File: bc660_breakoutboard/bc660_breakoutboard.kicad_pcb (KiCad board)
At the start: 2 copper layers, 22 parts, among them J2 Conn_01x12_Pin, J4 SIM8051-6-0-14-01-X-REVD, U1 BC660K-GL, U2 ESDS304DBVR

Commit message: update pcb design
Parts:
- added J1: SMA_CONNECTOR, SMA_CONNECTOR:LPRS_SMA_CONNECTOR, F.Cu at (125.4, 68.7)
- added J3: Conn_01x02_Pin, Connector_PinHeader_2.54mm:PinHeader_1x02_P2.54mm_Vertical, F.Cu at (101.3, 63.2)
- added J5: Conn_01x02_Pin, Connector_PinHeader_2.54mm:PinHeader_1x02_P2.54mm_Vertical, F.Cu at (112.8, 63.2)
- added J6: Conn_01x06_Pin, Connector_PinHeader_2.54mm:PinHeader_1x06_P2.54mm_Vertical, F.Cu at (103.9, 103.9)
- J2: value Conn_01x12_Pin -> Conn_01x01_Pin; footprint Connector_PinHeader_2.54mm:PinHeader_1x12_P2.54mm_Vertical -> Connector_PinHeader_2.54mm:PinHeader_1x01_P2.54mm_Vertical
- moved C6 85.1 mm to (107.1, 67.0), turned to -90 degrees
- moved C7 83.8 mm to (104.1, 67.0), turned to -90 degrees
- moved C8 82.7 mm to (101.1, 67.0), turned to -90 degrees
- moved C9 81.8 mm to (98.0, 67.0), turned to -90 degrees
- moved J2 68.7 mm to (92.2, 72.1), turned to 90 degrees
- moved C4 64.7 mm to (95.2, 94.0), turned to -90 degrees
- moved C5 57.8 mm to (88.4, 97.3), turned to -90 degrees
- moved J4 51.9 mm to (81.0, 88.4)
- moved C3 51.2 mm to (81.0, 105.2), turned to -90 degrees
- moved R4 33.2 mm to (72.4, 83.3)
- moved R2 32.3 mm to (81.0, 101.1), turned to 90 degrees
- moved R8 31.0 mm to (110.1, 67.1), turned to -90 degrees
- moved C2 30.8 mm to (75.7, 79.5), turned to 90 degrees
- moved R7 28.8 mm to (113.0, 67.1), turned to -90 degrees
- moved R1 27.1 mm to (78.5, 79.5), turned to -90 degrees
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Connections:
- C6 pad 2: Net-(J2-Pin_1) -> Net-(J3-Pin_2)
- C7 pad 2: Net-(J2-Pin_1) -> Net-(J3-Pin_2)
- C8 pad 2: Net-(J2-Pin_1) -> Net-(J3-Pin_2)
- C9 pad 2: Net-(J2-Pin_1) -> Net-(J3-Pin_2)
- R5 pad 1: Net-(J2-Pin_2) -> Net-(J6-Pin_4)
- R6 pad 1: Net-(J2-Pin_3) -> Net-(J6-Pin_3)
- R7 pad 1: Net-(J2-Pin_4) -> Net-(J5-Pin_1)
- R8 pad 1: Net-(J2-Pin_5) -> Net-(J5-Pin_2)
- R9 pad 2: Net-(J2-Pin_6) -> Net-(J6-Pin_6)
- U1 pad 15: Net-(J2-Pin_8) -> Net-(J6-Pin_1)
- U1 pad 16: GND -> Net-(J6-Pin_2)
- U1 pad 19: Net-(J2-Pin_9) -> Net-(J6-Pin_5)
- U1 pad 24: Net-(J2-Pin_10) -> unconnected-(U1-VDD_EXT-Pad24)
- U1 pad 42: Net-(J2-Pin_1) -> Net-(J3-Pin_2)
- U1 pad 43: Net-(J2-Pin_1) -> Net-(J3-Pin_2)
- U1 pad 7: Net-(J2-Pin_7) -> Net-(J2-Pin_1)
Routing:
- net Net-(U1-USIM_RST): track 0.00 -> 89.9 mm
- net Net-(J4-GND): track 0.00 -> 61.2 mm
- net Net-(J4-VCC): track 0.00 -> 50.2 mm
- net Net-(U1-USIM_DATA): track 0.00 -> 38.5 mm
- net Net-(J4-CLK): track 0.00 -> 22.7 mm
- net Net-(J3-Pin_2): track 0.00 -> 21.7 mm
- net Net-(J4-I/O): track 0.00 -> 19.3 mm
- net Net-(U1-USIM_CLK): track 0.00 -> 19.2 mm
- net Net-(J6-Pin_5): track 0.00 -> 15.0 mm
- net Net-(J2-Pin_1): track 0.00 -> 14.3 mm
- net Net-(J6-Pin_1): track 0.00 -> 14.2 mm
- net Net-(J6-Pin_2): track 0.00 -> 13.6 mm
- net Net-(U1-ANT_RF): track 0.00 -> 11.8 mm
- net Net-(U1-RI): track 0.00 -> 10.2 mm
- net Net-(U1-MAIN_RXD): track 0.00 -> 9.05 mm
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- added copper zone on B.Cu, net GND
- added copper zone on F.Cu, net GND
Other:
- board outline added: 59.7 x 48.5 mm

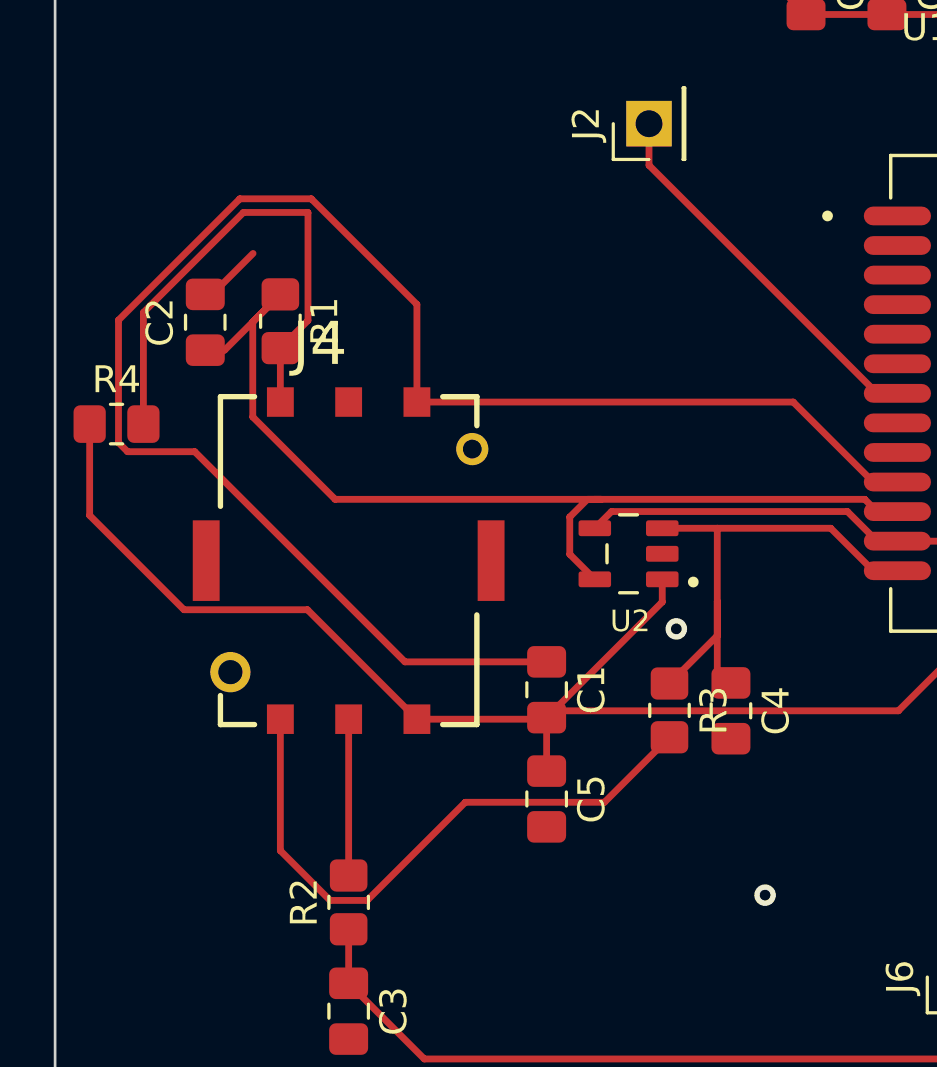
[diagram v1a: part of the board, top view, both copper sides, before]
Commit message: update pcb breakoutboard
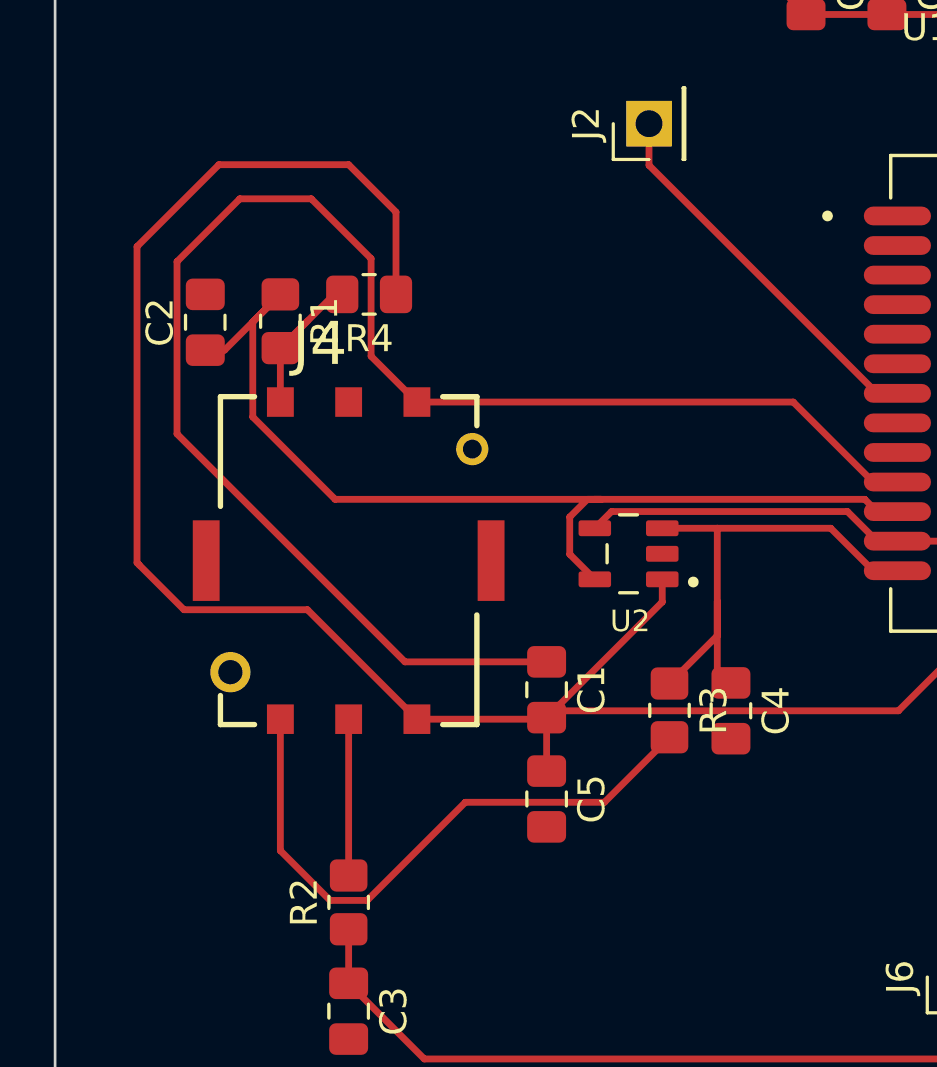
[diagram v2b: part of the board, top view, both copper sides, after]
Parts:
- moved R4 10.6 mm to (81.8, 78.5), turned to 180 degrees
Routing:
- net Net-(J4-VCC): track 50.2 -> 70.8 mm
- net Net-(J4-I/O): track 19.3 -> 6.59 mm
- net Net-(J4-GND): track 61.2 -> 57.9 mm
- net GND: track 5.42 -> 3.26 mm, vias 2 -> 0
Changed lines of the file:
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@@
   )
   (footprint "Resistor_SMD:R_0805_2012Metric_Pad1.20x1.40mm_HandSolder" (layer "F.Cu")
-    (at 72.39 83.312)
+    (at 81.788 78.486 180)
     (descr "Resistor SMD 0805 (2012 Metric), square (rectangular) end terminal, IPC_7351 nominal with elongated pad for handsoldering. (Body size source: IPC-SM-782 page 72, https://www.pcb-3d.com/wordpress/wp-content/uploads/ipc-sm-782a_amendment_1_and_2.pdf), generated with kicad-footprint-generator")
     (tags "resistor handsolder")
@@
     (fp_line (start 1 0.625) (end -1 0.625)
       (stroke (width 0.1) (type solid)) (layer "F.Fab"))
-    (pad "1" smd roundrect (at -1 0) (size 1.2 1.4) (layers "F.Cu" "F.Paste" "F.Mask") (roundrect_rratio 0.208333)
+    (pad "1" smd roundrect (at -1 0 180) (size 1.2 1.4) (layers "F.Cu" "F.Paste" "F.Mask") (roundrect_rratio 0.208333)
       (net 2 "Net-(J4-VCC)") (pintype "passive"))
-    (pad "2" smd roundrect (at 1 0) (size 1.2 1.4) (layers "F.Cu" "F.Paste" "F.Mask") (roundrect_rratio 0.208333)
+    (pad "2" smd roundrect (at 1 0 180) (size 1.2 1.4) (layers "F.Cu" "F.Paste" "F.Mask") (roundrect_rratio 0.208333)
       (net 45 "Net-(J4-I{slash}O)") (pintype "passive"))
     (model "${KICAD6_3DMODEL_DIR}/Resistor_SMD.3dshapes/R_0805_2012Metric.wrl"
@@
     (stroke (width 0.1) (type default)) (fill none) (layer "Edge.Cuts"))
   (segment (start 101.444 85.468) (end 100.544 85.468) (width 0.254) (layer "F.Cu") (net 1))
-  (segment (start 72.463 84.001001) (end 72.463 79.444447) (width 0.254) (layer "F.Cu") (net 1))
-  (segment (start 83.120999 92.159) (end 75.300999 84.339) (width 0.254) (layer "F.Cu") (net 1))
-  (segment (start 79.636052 74.93) (end 83.566 78.859948) (width 0.254) (layer "F.Cu") (net 1))
-  (segment (start 88.392 92.159) (end 83.120999 92.159) (width 0.254) (layer "F.Cu") (net 1))
-  (segment (start 72.800999 84.339) (end 72.463 84.001001) (width 0.254) (layer "F.Cu") (net 1))
+  (segment (start 79.636052 74.93) (end 76.977447 74.93) (width 0.254) (layer "F.Cu") (net 1))
+  (segment (start 83.120999 92.159) (end 88.392 92.159) (width 0.254) (layer "F.Cu") (net 1))
+  (segment (start 74.64 77.267448) (end 74.64 83.678) (width 0.254) (layer "F.Cu") (net 1))
+  (segment (start 76.977447 74.93) (end 74.64 77.267448) (width 0.254) (layer "F.Cu") (net 1))
+  (segment (start 81.861 77.154948) (end 79.636052 74.93) (width 0.254) (layer "F.Cu") (net 1))
+  (segment (start 81.861 80.787) (end 81.861 77.154948) (width 0.254) (layer "F.Cu") (net 1))
   (segment (start 100.544 85.468) (end 97.568 82.492) (width 0.254) (layer "F.Cu") (net 1))
-  (segment (start 75.300999 84.339) (end 72.800999 84.339) (width 0.254) (layer "F.Cu") (net 1))
-  (segment (start 72.463 79.444447) (end 76.977447 74.93) (width 0.254) (layer "F.Cu") (net 1))
+  (segment (start 74.64 83.678) (end 83.120999 92.159) (width 0.254) (layer "F.Cu") (net 1))
+  (segment (start 83.566 82.492) (end 81.861 80.787) (width 0.254) (layer "F.Cu") (net 1))
   (segment (start 97.568 82.492) (end 83.566 82.492) (width 0.254) (layer "F.Cu") (net 1))
-  (segment (start 83.566 78.859948) (end 83.566 82.492) (width 0.254) (layer "F.Cu") (net 1))
-  (segment (start 76.977447 74.93) (end 79.636052 74.93) (width 0.254) (layer "F.Cu") (net 1))
+  (segment (start 81.026 73.66) (end 82.788 75.422) (width 0.254) (layer "F.Cu") (net 2))
   (segment (start 88.392 94.234) (end 88.392 96.223) (width 0.254) (layer "F.Cu") (net 2))
   (segment (start 88.334 94.292) (end 88.392 94.234) (width 0.254) (layer "F.Cu") (net 2))
   (segment (start 88.646 93.98) (end 88.392 94.234) (width 0.254) (layer "F.Cu") (net 2))
   (segment (start 92.695 89.931) (end 88.392 94.234) (width 0.254) (layer "F.Cu") (net 2))
+  (segment (start 73.239 88.559) (end 73.152 88.472) (width 0.254) (layer "F.Cu") (net 2))
   (segment (start 83.566 94.292) (end 79.493 90.219) (width 0.254) (layer "F.Cu") (net 2))
+  (segment (start 74.899 90.219) (end 73.239 88.559) (width 0.254) (layer "F.Cu") (net 2))
   (segment (start 101.482 93.98) (end 88.646 93.98) (width 0.254) (layer "F.Cu") (net 2))
   (segment (start 92.695 89.088) (end 92.695 89.931) (width 0.254) (layer "F.Cu") (net 2))
   (segment (start 79.493 90.219) (end 74.899 90.219) (width 0.254) (layer "F.Cu") (net 2))
   (segment (start 104.694 90.768) (end 101.482 93.98) (width 0.254) (layer "F.Cu") (net 2))
+  (segment (start 73.152 76.708) (end 76.2 73.66) (width 0.254) (layer "F.Cu") (net 2))
   (segment (start 83.566 94.292) (end 88.334 94.292) (width 0.254) (layer "F.Cu") (net 2))
-  (segment (start 74.899 90.219) (end 71.39 86.71) (width 0.254) (layer "F.Cu") (net 2))
-  (segment (start 71.39 86.71) (end 71.39 83.312) (width 0.254) (layer "F.Cu") (net 2))
+  (segment (start 76.2 73.66) (end 81.026 73.66) (width 0.254) (layer "F.Cu") (net 2))
+  (segment (start 82.788 75.422) (end 82.788 78.486) (width 0.254) (layer "F.Cu") (net 2))
+  (segment (start 73.152 88.472) (end 73.152 76.708) (width 0.254) (layer "F.Cu") (net 2))
   (segment (start 100.230577 86.112) (end 100.686577 86.568) (width 0.254) (layer "F.Cu") (net 3))
   (segment (start 75.692 80.561) (end 76.411 80.561) (width 0.254) (layer "F.Cu") (net 3))
@@
   (segment (start 98.044 65.997) (end 101.054 65.997) (width 0.254) (layer "F.Cu") (net 4))
   (segment (start 75.692 78.486) (end 75.946 78.486) (width 0.254) (layer "F.Cu") (net 4))
-  (segment (start 75.946 78.486) (end 77.47 76.962) (width 0.254) (layer "F.Cu") (net 4))
-  (via (at 93.218 90.932) (size 0.8) (drill 0.4) (layers "F.Cu" "B.Cu") (free) (net 4))
-  (via (at 96.52 100.838) (size 0.8) (drill 0.4) (layers "F.Cu" "B.Cu") (free) (net 4))
   (segment (start 83.8415 106.934) (end 81.026 104.1185) (width 0.254) (layer "F.Cu") (net 5))
   (segment (start 113.786577 87.668) (end 121.158 95.039423) (width 0.254) (layer "F.Cu") (net 5))
@@
   (segment (start 116.586 98.806) (end 111.294 93.514) (width 0.254) (layer "F.Cu") (net 15))
   (segment (start 111.294 93.514) (end 111.294 90.768) (width 0.254) (layer "F.Cu") (net 15))
-  (segment (start 79.502 75.438) (end 77.111499 75.438) (width 0.254) (layer "F.Cu") (net 45))
-  (segment (start 79.513 79.459) (end 79.513 75.449) (width 0.254) (layer "F.Cu") (net 45))
-  (segment (start 79.513 75.449) (end 79.502 75.438) (width 0.254) (layer "F.Cu") (net 45))
+  (segment (start 80.486 78.486) (end 78.486 80.486) (width 0.25) (layer "F.Cu") (net 45))
+  (segment (start 80.788 78.486) (end 80.486 78.486) (width 0.25) (layer "F.Cu") (net 45))
   (segment (start 78.486 80.486) (end 79.513 79.459) (width 0.254) (layer "F.Cu") (net 45))
   (segment (start 78.486 82.492) (end 78.486 80.486) (width 0.254) (layer "F.Cu") (net 45))
-  (segment (start 73.39 79.159499) (end 73.39 83.312) (width 0.254) (layer "F.Cu") (net 45))
-  (segment (start 77.111499 75.438) (end 73.39 79.159499) (width 0.254) (layer "F.Cu") (net 45))
   (segment (start 116.744 74.964) (end 123.014 68.694) (width 0.254) (layer "F.Cu") (net 46))
   (segment (start 116.744 75.568) (end 116.744 74.964) (width 0.254) (layer "F.Cu") (net 46))
